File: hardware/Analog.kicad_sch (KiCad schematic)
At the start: 66 parts, among them J1 PH1-03-UA, J10 PinHeader 02x04, J11 PinHeader 02x04, J12 PH1-03-UA, J2 PinHeader 02x04, J3 PinHeader 02x04, J4 PH1-03-UA, J5 PH1-03-UA, J6 PinHeader 02x04, J7 PinHeader 02x04, J8 PH1-03-UA, J9 PH1-03-UA, U11 TLC274AIDR, U12 INA2128UA_1K, U13 TLC274AIDR, U14 TLC274AIDR, U15 INA2128UA_1K, U16 INA2128UA_1K

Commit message: Preliminary components placement
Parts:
- removed J10, J11, J2, J3, J6, J7: PinHeader 02x04, Connector_PinHeader_2.54mm:PinHeader_2x04_P2.54mm_Vertical, symbol Connector_Generic:Conn_02x04_Counter_Clockwise
- added J1, J2, J3, J4, J5, J6: PinHeader 02x04, Connector_PinHeader_2.54mm:PinHeader_2x04_P2.54mm_Vertical, symbol PINHEADER_02x04:PinHeader_02x04
- renumbered C42 to C39, C39 to C40, C40 to C41, C41 to C42, J8 to J10, J9 to J11, J1 to J7, J4 to J8, J5 to J9, R15 to R14, R16 to R15, R17 to R16, R19 to R17, R21 to R18, R23 to R19, R24 to R20, R25 to R21, R29 to R22, R30 to R23, R31 to R24, R33 to R25, R35 to R26, R37 to R27, R38 to R28, R39 to R29, R43 to R30, R44 to R31, R45 to R32, R47 to R33, R49 to R34, R51 to R35, R52 to R36, R53 to R37, R14 to R38, R18 to R39, R20 to R40, R22 to R41, R26 to R42, R27 to R43, R28 to R44, R32 to R45, R34 to R46, R36 to R47, R40 to R48, R41 to R49, R42 to R50, R46 to R51, R48 to R52, R50 to R53, U12 to U11, U15 to U12, U16 to U13, U13 to U15, U11 to U15, U13 to U16, U11 to U16
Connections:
- net DIF5: now also U14.12 (+), U14.14; no longer U14.10 (+), U14.8
- net DIF6: now also U14.10 (+), U14.8; no longer U14.12 (+), U14.14
- net RGA1_2: now also J1.2 (Pin_8), J1.4 (Pin_7), J1.6 (Pin_6), J1.8 (Pin_5)
- net RGA2_2: now also J2.2 (Pin_8), J2.4 (Pin_7), J2.6 (Pin_6), J2.8 (Pin_5)
- net RGA3_2: now also J3.2 (Pin_8), J3.4 (Pin_7), J3.6 (Pin_6), J3.8 (Pin_5)
- net RGA4_2: now also J4.2 (Pin_8), J4.4 (Pin_7), J4.6 (Pin_6), J4.8 (Pin_5)
- net RGA5_2: now also J5.2 (Pin_8), J5.4 (Pin_7), J5.6 (Pin_6), J5.8 (Pin_5)
- net RGA6_2: now also J6.2 (Pin_8), J6.4 (Pin_7), J6.6 (Pin_6), J6.8 (Pin_5)
- net SE1: now also U16.5 (+), U16.7; no longer U16.1, U16.3 (+)
- net SE1IN: now also U16.6 (-); no longer U16.2 (-)
- net SE2: now also U16.1, U16.3 (+); no longer U16.5 (+), U16.7
- net SE2IN: now also U16.2 (-); no longer U16.6 (-)
- net SE3: now also U16.12 (+), U16.14; no longer U16.10 (+), U16.8
- net SE3IN: now also U16.13 (-); no longer U16.9 (-)
- net SE4: now also U15.1, U15.3 (+); no longer U15.12 (+), U15.14
- net SE4IN: now also U15.2 (-); no longer U15.13 (-)
- net SE5: now also U15.5 (+), U15.7; no longer U15.1, U15.3 (+)
- net SE5IN: now also U15.6 (-); no longer U15.2 (-)
- net SE6: now also U15.10 (+), U15.8; no longer U15.5 (+), U15.7
- net SE6IN: now also U15.9 (-); no longer U15.6 (-)
- net at R22.1: now also J3.1 (Pin_1)
- net at R21.1: now also J2.7 (Pin_4)
- net at R33.1: now also J5.7 (Pin_4)
- net at R37.1: now also J6.7 (Pin_4)
- net at R53.1, R54.2, R55.1: now also U14.9 (-); no longer U14.13 (-)
- net at R30.1: now also J5.1 (Pin_1)
- net at R31.1: now also J5.3 (Pin_2)
- net at R32.1: now also J5.5 (Pin_3)
- net at R24.1: now also J3.5 (Pin_3)
- net at R36.1: now also J6.5 (Pin_3)
- net at R23.1: now also J3.3 (Pin_2)
- net at R25.1: now also J3.7 (Pin_4)
- net at R27.1: now also J4.3 (Pin_2)
- net at R50.1, R51.2, R52.1: now also U14.13 (-); no longer U14.9 (-)
- net at R34.1: now also J6.1 (Pin_1)
- net at R35.1: now also J6.3 (Pin_2)
- net at R17.1: now also J1.7 (Pin_4)
- net at R26.1: now also J4.1 (Pin_1)
- net at R14.1: now also J1.1 (Pin_1)
- net at R28.1: now also J4.5 (Pin_3)
- net at R29.1: now also J4.7 (Pin_4)
- net at R20.1: now also J2.5 (Pin_3)
- net at R18.1: now also J2.1 (Pin_1)
- net at R19.1: now also J2.3 (Pin_2)
- net at R16.1: now also J1.5 (Pin_3)
- net at R15.1: now also J1.3 (Pin_2)
- net +5V renamed +5VA

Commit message: Finished components placement on PCB
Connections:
- net DIF3+: now also U12.1 (V-INA); no longer U12.2 (V+INA)
- net DIF3-: now also U12.2 (V+INA); no longer U12.1 (V-INA)
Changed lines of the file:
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@@
 		(stroke
 			(width 0)
-			(type solid)
+			(type dash_dot)
 		)
 		(fill
@@
 	(rectangle
 		(start 242.57 176.784)
-		(end 323.342 221.742)
+		(end 323.342 220.218)
 		(stroke
 			(width 0)
-			(type solid)
+			(type dash_dot)
 		)
 		(fill
@@
 	)
 	(rectangle
-		(start 242.57 19.558)
-		(end 406.4 127.762)
+		(start 242.57 20.32)
+		(end 406.4 126.492)
 		(stroke
 			(width 0)
-			(type solid)
+			(type dash_dot)
 		)
 		(fill
@@
 		)
 	)
-	(label "DIF3+"
+	(label "DIF3-"
 		(at 33.02 121.92 0)
 		(effects
@@
 		)
 	)
-	(label "DIF3-"
+	(label "DIF3+"
 		(at 33.02 119.38 0)
 		(effects

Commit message: Finished routing on PCB
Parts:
- added TP10, TP11, TP12, TP13, TP14, TP15, TP16, TP17, TP18, TP19, TP8, TP9: TestPoint_Small, TestPoint:TestPoint_THTPad_D1.0mm_Drill0.5mm, symbol Connector:TestPoint_Small
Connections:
- net DIF1: now also TP8.1
- net DIF2: now also TP9.1
- net DIF3: now also TP10.1
- net DIF3+: now also U12.2 (V+INA); no longer U12.1 (V-INA)
- net DIF3-: now also U12.1 (V-INA); no longer U12.2 (V+INA)
- net DIF4: now also TP11.1
- net DIF5: now also TP12.1
- net DIF6: now also TP13.1
- net SE1: now also TP14.1
- net SE2: now also TP15.1
- net SE3: now also TP16.1
- net SE4: now also TP17.1
- net SE5: now also TP18.1
- net SE6: now also TP19.1

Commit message: Added all missing datasheet links etc
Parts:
- J10, J11, J12, J7, J8, J9: Manufacturer_Part_Number (none) -> PH1-03-UA; Mouser (none) -> https://www.mouser.pl/ProductDetail/Adam-Tech/PH1-03-UA?qs=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; Mouser No (none) -> 737-PH1-03-UA
- R39, R42, R45, R48, R51, R54: Manufacturer_Part_Number (none) -> CRCW06030000Z0EAHP; Mouser in warszatowe zapasy i think -> https://www.mouser.pl/ProductDetail/Vishay/CRCW06030000Z0EA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; Mouser No (none) -> 71-CRCW06030000Z0EAH
- R40, R43, R46, R49, R52, R55: Manufacturer_Part_Number (none) -> AC0603JR-0710KL; Mouser in warszatowe zapasy i think -> https://www.mouser.pl/ProductDetail/YAGEO/AC0603JR-0710KL?q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; Mouser No (none) -> 603-AC0603JR-0710KL
- TP10, TP11, TP12, TP13, TP14, TP15, TP16, TP17, TP18, TP19, TP8, TP9: Manufacturer_Part_Number (none) -> ---; Mouser (none) -> ---; Mouser No (none) -> ---

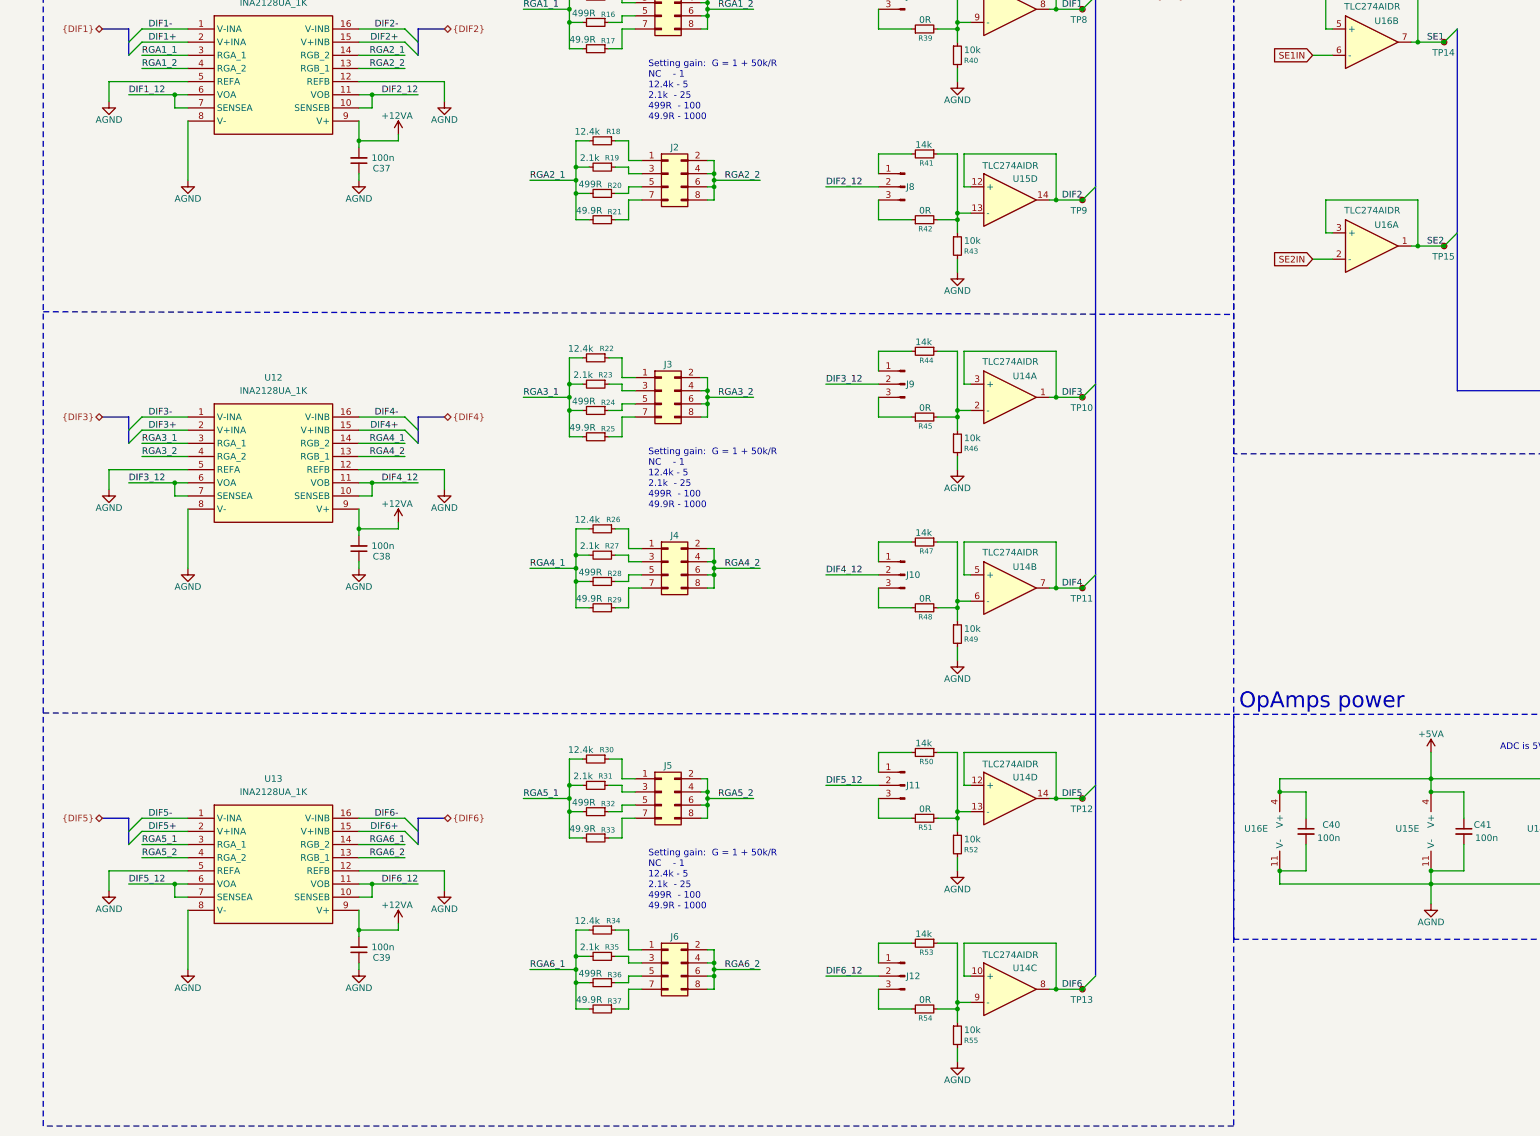
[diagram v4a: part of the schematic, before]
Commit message: Corrections after review
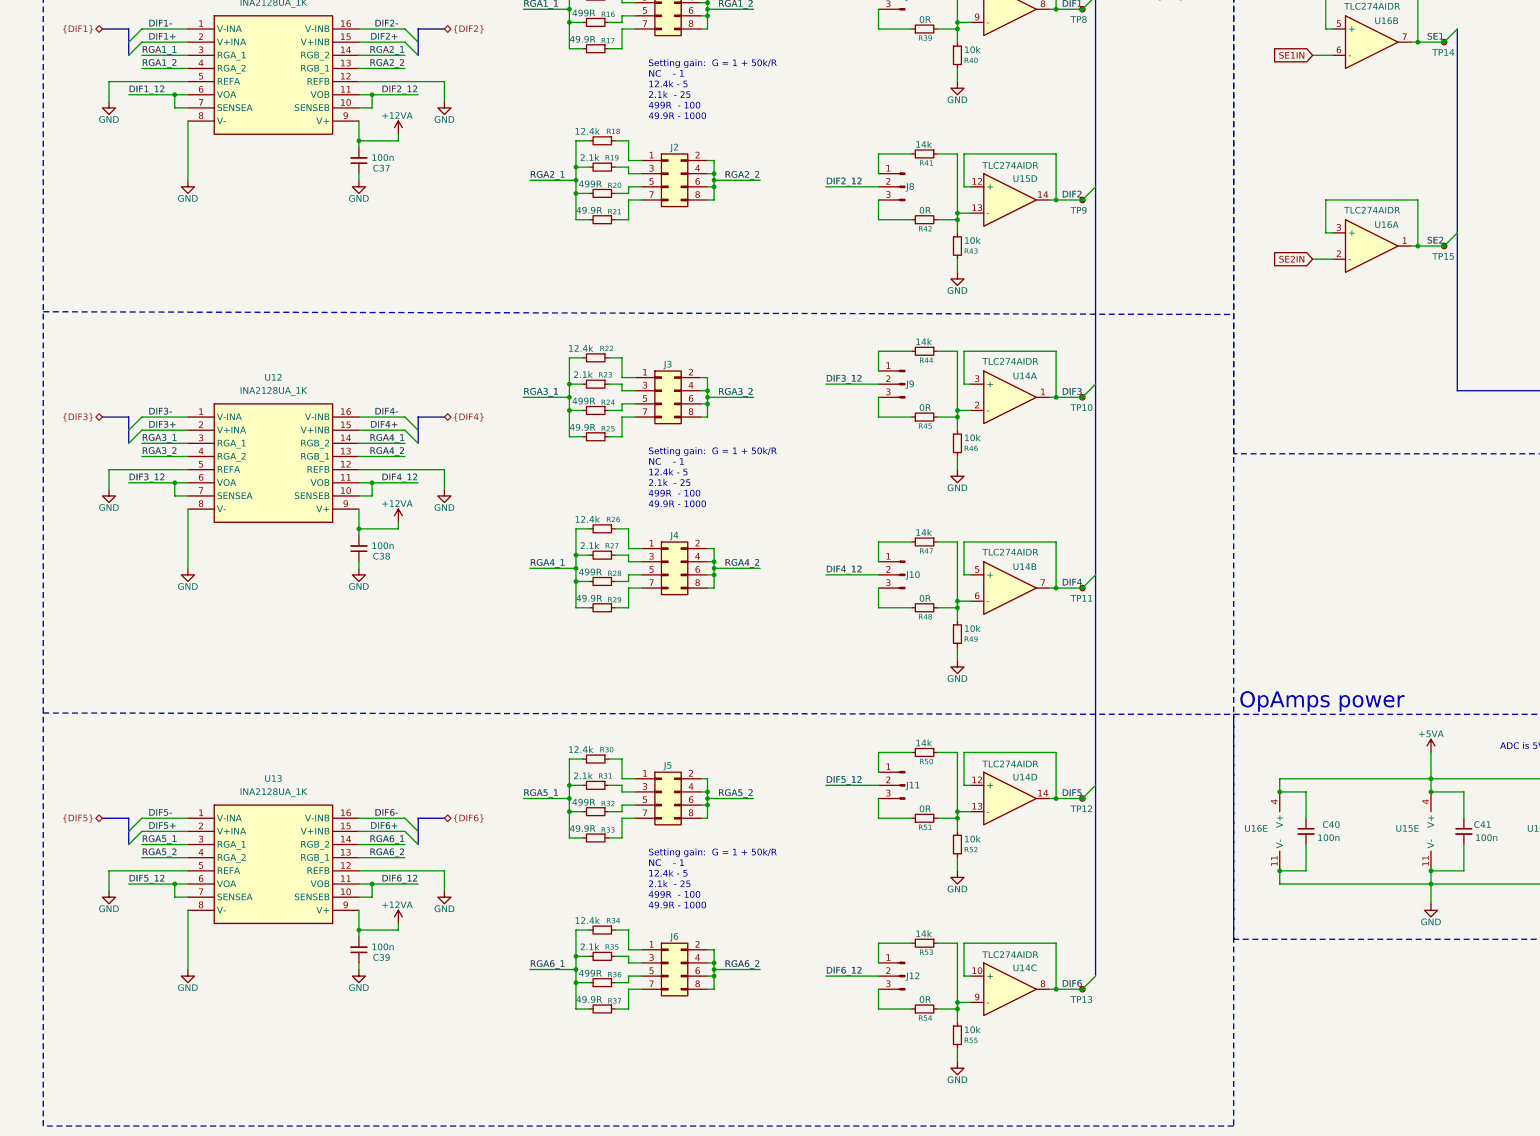
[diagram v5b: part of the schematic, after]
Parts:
- J10, J11, J12, J7, J8, J9: Manufacturer_Part_Number PH1-03-UA -> (none); Mouser https://www.mouser.pl/ProductDetail/Adam-Tech/PH1-03-UA?qs=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 -> (none); Mouser No 737-PH1-03-UA -> (none)
- R39, R42, R45, R48, R51, R54: Manufacturer_Part_Number CRCW06030000Z0EAHP -> (none); Mouser https://www.mouser.pl/ProductDetail/Vishay/CRCW06030000Z0EA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 -> in warszatowe zapasy i think; Mouser No 71-CRCW06030000Z0EAH -> (none)
- R40, R43, R46, R49, R52, R55: Manufacturer_Part_Number AC0603JR-0710KL -> (none); Mouser https://www.mouser.pl/ProductDetail/YAGEO/AC0603JR-0710KL?q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 -> in warszatowe zapasy i think; Mouser No 603-AC0603JR-0710KL -> (none)
- TP10, TP11, TP12, TP13, TP14, TP15, TP16, TP17, TP18, TP19, TP8, TP9: Manufacturer_Part_Number --- -> (none); Mouser --- -> (none); Mouser No --- -> (none)
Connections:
- net AGND renamed GND

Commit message: Added Voltage reference, fixed silkscreen and BOM
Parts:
- added R56: 2.1k, Resistor_SMD:R_0603_1608Metric_Pad0.98x0.95mm_HandSolder, symbol Device:R_Small
- added R57, R58: 10k, Resistor_SMD:R_0603_1608Metric_Pad0.98x0.95mm_HandSolder, symbol Device:R_Small
- added U17: TL431LIBQDBZRQ1, Package_TO_SOT_SMD:SOT-23W_Handsoldering, symbol Reference_Voltage:TL431DBZ
- J10, J11, J12, J7, J8, J9: Manufacturer_Part_Number (none) -> PH1-03-UA; Mouser (none) -> https://www.mouser.pl/ProductDetail/Adam-Tech/PH1-03-UA?qs=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; Mouser No (none) -> 737-PH1-03-UA
- R39, R42, R45, R48, R51, R54: Manufacturer_Part_Number (none) -> CRCW06030000Z0EAHP; Mouser in warszatowe zapasy i think -> https://www.mouser.pl/ProductDetail/Vishay/CRCW06030000Z0EA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; Mouser No (none) -> 71-CRCW06030000Z0EAH
- R40: Manufacturer_Part_Number (none) -> AC0603JR-0710KL; Mouser in warszatowe zapasy i think -> https://www.mouser.pl/ProductDetail/YAGEO/AC0603JR-0710KL?q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; Mouser No (none) -> 603-AC0603JR-0710KL603-AC0603JR-0710KL
- R43, R46, R49, R52, R55: Manufacturer_Part_Number (none) -> AC0603JR-0710KL; Mouser in warszatowe zapasy i think -> https://www.mouser.pl/ProductDetail/YAGEO/AC0603JR-0710KL?q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; Mouser No (none) -> 603-AC0603JR-0710KL
- U11, U12, U13: footprint SOIC127P1030X265-16N -> difopamp:SOIC127P1030X265-16N
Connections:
- net +12VA: now also R56.2
- net GND: now also R58.2, U17.3 (A); no longer U11.12 (REFB), U11.5 (REFA), U12.12 (REFB), U12.5 (REFA), U13.12 (REFB), U13.5 (REFA)
- new net: R57.2, R58.1, U17.2 (REF)
- new net +6VA: R56.1, R57.1, U11.12 (REFB), U11.5 (REFA), U12.12 (REFB), U12.5 (REFA), U13.12 (REFB), U13.5 (REFA), U17.1 (K)

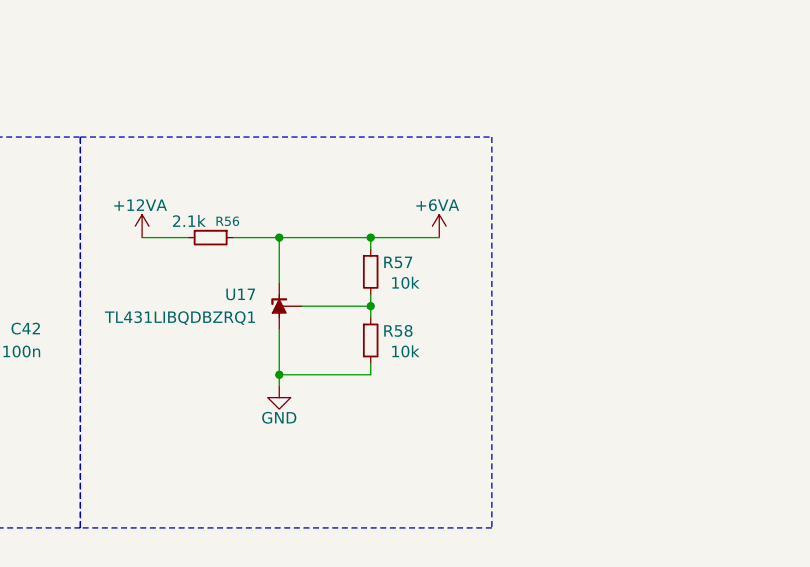
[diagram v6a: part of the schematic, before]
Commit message: Fixed R57 value
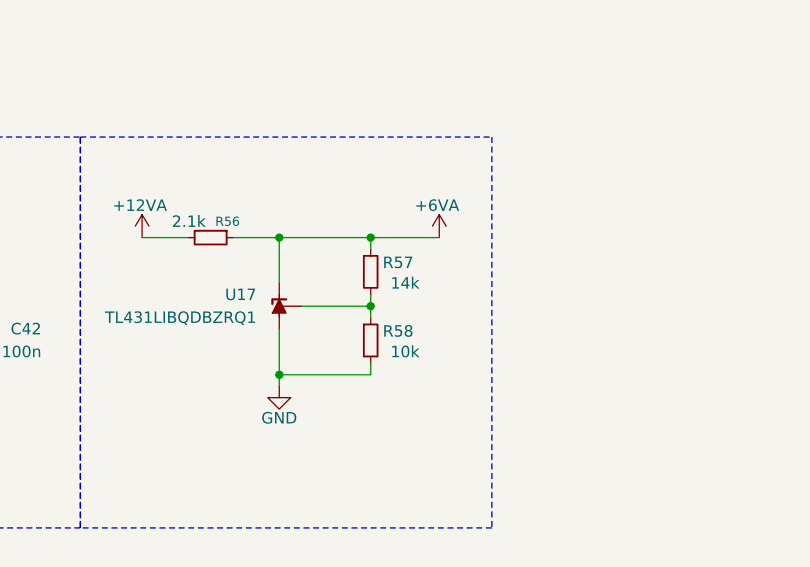
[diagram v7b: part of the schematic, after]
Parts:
- R57: value 10k -> 14k; Manufacturer_Part_Number MCT0603MG1002BP500 -> MCT06030E1402BP500; Mouser https://www.mouser.pl/ProductDetail/Vishay-Beyschlag/MCT0603MG1002BP500?qs=sGAEpiMZZMvdGkrng054tzrpBd13L%252B8iZRtTSmMrLrPwCtwKU%2F2taw%3D%3D -> https://www.mouser.pl/ProductDetail/Vishay-Beyschlag/MCT06030E1402BP500?qs=sGAEpiMZZMvdGkrng054t1rYBQGPYet6PJmZ5%252BgnwgY%3D; Mouser No 594-MCT0603MG1002BP5 -> 594-MCT06030E1402BP5
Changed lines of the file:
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@@
 			)
 		)
-		(property "Value" "10k"
+		(property "Value" "14k"
 			(at 359.41 193.04 0)
 			(effects
@@
 			)
 		)
-		(property "Datasheet" "https://www.vishay.com/docs/28952/mcr0201at-mca1206at.pdf"
+		(property "Datasheet" "https://www.vishay.com/docs/28700/mcx0x0xpre.pdf"
 			(at 355.6 191.77 0)
 			(effects
@@
 			)
 		)
-		(property "Mouser" "https://www.mouser.pl/ProductDetail/Vishay-Beyschlag/MCT0603MG1002BP500?qs=sGAEpiMZZMvdGkrng054tzrpBd13L%252B8iZRtTSmMrLrPwCtwKU%2F2taw%3D%3D"
+		(property "Mouser" "https://www.mouser.pl/ProductDetail/Vishay-Beyschlag/MCT06030E1402BP500?qs=sGAEpiMZZMvdGkrng054t1rYBQGPYet6PJmZ5%252BgnwgY%3D"
 			(at 355.6 191.77 0)
 			(effects
@@
 			)
 		)
-		(property "Mouser No" "594-MCT0603MG1002BP5"
+		(property "Mouser No" "594-MCT06030E1402BP5"
 			(at 355.6 191.77 0)
 			(effects
@@
 			)
 		)
-		(property "Manufacturer_Part_Number" "MCT0603MG1002BP500"
+		(property "Manufacturer_Part_Number" "MCT06030E1402BP500"
 			(at 355.6 191.77 0)
 			(effects

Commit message: Changed some components - they were non stocked
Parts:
- J1, J2, J3, J4, J5, J6: value PinHeader 02x04 -> PH2-04-UA
- R17, R21, R25, R29, R33, R37: Manufacturer_Part_Number ERA-3AEB49R9V -> CRT0603ABY-49R9ELF; Mouser https://www.mouser.pl/ProductDetail/Panasonic/ERA-3AEB49R9V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 -> https://www.mouser.pl/ProductDetail/Bourns/CRT0603ABY-49R9E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; Mouser No 667-ERA-3AEB49R9V -> 652-CRT0603ABY-49R9E
- R40: Manufacturer_Part_Number AC0603JR-0710KL -> RE0603FRE0710KL; Mouser https://www.mouser.pl/ProductDetail/YAGEO/AC0603JR-0710KL?q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 -> https://www.mouser.pl/ProductDetail/YAGEO/RE0603FRE0710KL?q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; Mouser No 603-AC0603JR-0710KL603-AC0603JR-0710KL -> 603-RE0603FRE0710KL
- R43, R46, R49, R52, R55: Manufacturer_Part_Number AC0603JR-0710KL -> RE0603FRE0710KL; Mouser https://www.mouser.pl/ProductDetail/YAGEO/AC0603JR-0710KL?q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 -> https://www.mouser.pl/ProductDetail/YAGEO/RE0603FRE0710KL?q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; Mouser No 603-AC0603JR-0710KL -> 603-RE0603FRE0710KL
- R58: Manufacturer_Part_Number MCT0603MG1002BP500 -> ERA-3APB103V; Mouser https://www.mouser.pl/ProductDetail/Vishay-Beyschlag/MCT060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 -> https://www.mouser.pl/ProductDetail/Panasonic/ERA-3APB103V?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; Mouser No 594-MCT0603MG1002BP5 -> 667-ERA-3APB103V
